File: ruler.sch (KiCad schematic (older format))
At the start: 80 parts, among them J1 USB_OTG, Q1 SOT23, Q2 SOT323, Q3 SOT883, Q4 SOT523, Q5 SOT223, Q6 SOT89, Q7 SuperSOT, SW1 KMR2, SW2 EVQPE1, SW3 B3U1000P, SW4 FSMCT, SW5 TL3315, SW6 FSM2JSM, SW7 JS202011SCQN, U1 QFN-0.5mm, U10 SOT963-6, U11 SSOP14, U12 SO16-L, U13 SOT666, U14 SOT1194, U15 SOT1333, U16 SOT669, U17 TSSOP 4.4x3mm, U18 SO4, U19 VSSOP, U2 LQFP, U3 SOIC, U4 BGA-0.8mm, U5 TSSOP 3x3mm, U6 MSOIC, U7 TSOP-0.95mm, U8 SOT23-6, U9 SOT23-8

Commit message: Add another switch
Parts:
- added LED?: 0201, KiCad/LEDs.pretty:LED_0201, symbol device:LED
- added R?: 1k, KiCad/Resistors_SMD.pretty:R_0402, symbol device:R
- added SW?: B3U, KiCad/Buttons_Switches_SMD.pretty:SW_SPST_EVQPE1, symbol switches:SW_Push
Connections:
- wire segments 78 -> 87
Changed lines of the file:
@@
 L device:D D5
 U 1 1 5AF4E276
-P 9625 1300
-F 0 "D5" V 9671 1221 50  0000 R CNN
-F 1 "SOD-323" V 9580 1221 50  0000 R CNN
-F 2 "KiCad/Diodes_SMD.pretty:D_SOD-323" H 9625 1300 50  0001 C CNN
-F 3 "" H 9625 1300 50  0001 C CNN
-	1    9625 1300
+P 4800 2750
+F 0 "D5" V 4846 2671 50  0000 R CNN
+F 1 "SOD-323" V 4755 2671 50  0000 R CNN
+F 2 "KiCad/Diodes_SMD.pretty:D_SOD-323" H 4800 2750 50  0001 C CNN
+F 3 "" H 4800 2750 50  0001 C CNN
+	1    4800 2750
 	0    -1   -1   0
 $EndComp
@@
 	1    0    0    -1
 $EndComp
+$Comp
+L device:R R?
+U 1 1 5B70AFDC
+P 4650 3150
+F 0 "R?" V 4730 3150 50  0000 C CNN
+F 1 "1k" V 4650 3150 50  0000 C CNN
+F 2 "KiCad/Resistors_SMD.pretty:R_0402" V 4580 3150 50  0001 C CNN
+F 3 "" H 4650 3150 50  0001 C CNN
+	1    4650 3150
+	1    0    0    -1
+$EndComp
+$Comp
+L device:LED LED?
+U 1 1 5B70AFE2
+P 4650 3575
+F 0 "LED?" H 4650 3675 50  0000 C CNN
+F 1 "0201" H 4650 3475 50  0000 C CNN
+F 2 "KiCad/LEDs.pretty:LED_0201" H 4650 3575 50  0001 C CNN
+F 3 "" H 4650 3575 50  0001 C CNN
+	1    4650 3575
+	0    -1   -1   0
+$EndComp
+$Comp
+L power:GND #PWR?
+U 1 1 5B70AFE8
+P 4650 3850
+F 0 "#PWR?" H 4650 3600 50  0001 C CNN
+F 1 "GND" H 4650 3700 50  0000 C CNN
+F 2 "" H 4650 3850 50  0001 C CNN
+F 3 "" H 4650 3850 50  0001 C CNN
+	1    4650 3850
+	1    0    0    -1
+$EndComp
+Wire Wire Line
+	4650 3725 4650 3850
+Wire Wire Line
+	4650 2925 4650 3000
+$Comp
+L switches:SW_Push SW?
+U 1 1 5B70AFF0
+P 4375 2925
+F 0 "SW?" H 4425 3025 50  0000 L CNN
+F 1 "B3U" H 4375 2865 50  0000 C CNN
+F 2 "KiCad/Buttons_Switches_SMD.pretty:SW_SPST_EVQPE1" H 4375 3125 50  0001 C CNN
+F 3 "" H 4375 3125 50  0001 C CNN
+	1    4375 2925
+	1    0    0    -1
+$EndComp
+Text GLabel 4100 2925 0    50   Input ~ 0
+SW_V+
+Wire Wire Line
+	4100 2925 4150 2925
+Text GLabel 4800 2400 1    50   Input ~ 0
+LED_V+
+Connection ~ 4150 2925
+Connection ~ 4575 2925
+Wire Wire Line
+	4575 2925 4650 2925
+Wire Wire Line
+	4800 2400 4800 2600
+Wire Wire Line
+	4800 2900 4800 2925
+Wire Wire Line
+	4800 2925 4650 2925
+Connection ~ 4650 2925
+Wire Wire Line
+	4650 3300 4650 3425
+Wire Wire Line
+	4175 2925 4150 2925
 $EndSCHEMATC

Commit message: Convert to kicad-5 properly?
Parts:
- C1, C2, C3, C4, C5, C6, C7, C8: symbol device:CP -> ruler-rescue:device_CP
- D1, D2, D3, D4, D5, D6: symbol device:D -> ruler-rescue:device_D
- DRAWING1, DRAWING10, DRAWING11, DRAWING12, DRAWING13, DRAWING14, DRAWING15, DRAWING16, DRAWING17, DRAWING18, DRAWING2, DRAWING3, DRAWING4, DRAWING5, DRAWING6, DRAWING9, U1, U10, U11, U12, U13, U14, U15, U16, U17, U18, U19, U2, U3, U4, U5, U6, U7, U8, U9: symbol conn:Conn_01x01 -> ruler-rescue:conn_Conn_01x01
- J1: symbol conn:USB_OTG -> ruler-rescue:conn_USB_OTG
- L1, L2, L3, L4, L5, L6: symbol pspice:INDUCTOR -> ruler-rescue:pspice_INDUCTOR
- LED1, LED2, LED3, LED4, LED5: symbol device:LED -> ruler-rescue:device_LED
- LED6: renamed from LED?; footprint KiCad/LEDs.pretty:LED_0201 -> KiCad/kicad-footprints/LED_SMD.pretty:LED_0201_0603Metric; symbol device:LED -> ruler-rescue:device_LED
- Q1, Q2, Q3, Q4, Q5, Q6, Q7: symbol device:Q_NMOS_DGS -> ruler-rescue:device_Q_NMOS_DGS
- R1, R2, R3, R4, R5: symbol device:R -> ruler-rescue:device_R
- R6: renamed from R?; footprint KiCad/Resistors_SMD.pretty:R_0402 -> KiCad/kicad-footprints/Resistor_SMD.pretty:R_01005_0402Metric; symbol device:R -> ruler-rescue:device_R
- SW1, SW2, SW3, SW6: symbol switches:SW_Push -> ruler-rescue:switches_SW_Push
- SW4, SW5: symbol switches:SW_Push_Dual -> ruler-rescue:switches_SW_Push_Dual
- SW7: symbol Switch:SW_DPDT_x2 -> ruler-rescue:Switch_SW_DPDT_x2
- SW8: renamed from SW?; symbol switches:SW_Push -> ruler-rescue:switches_SW_Push
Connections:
- wire segments 87 -> 86

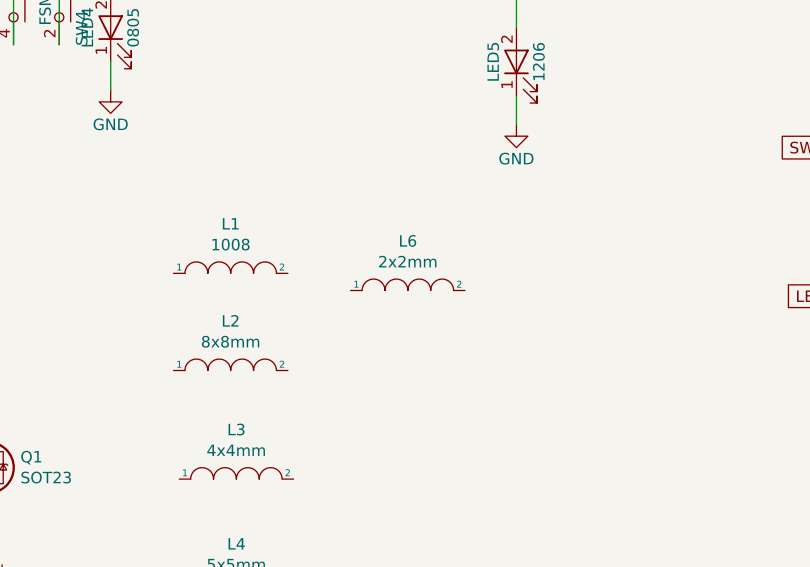
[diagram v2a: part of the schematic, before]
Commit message: Add a tactile switch and 0201 LED
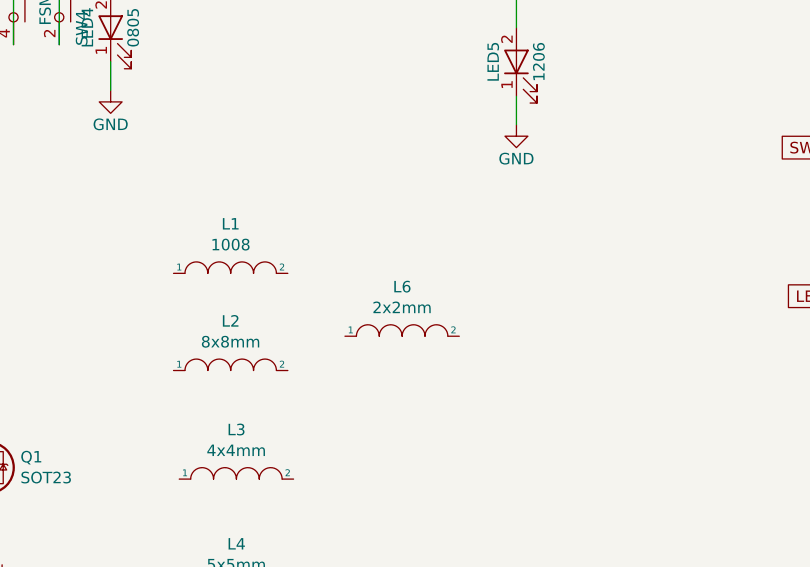
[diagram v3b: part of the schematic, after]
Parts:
- SW8: footprint KiCad/Buttons_Switches_SMD.pretty:SW_SPST_EVQPE1 -> brunoeagle/kicad-open-modules:B3U-1000P
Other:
- moved on the sheet: L6
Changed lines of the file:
@@
 L ruler-rescue:pspice_INDUCTOR L6
 U 1 1 5AF4B711
-P 8450 3125
-F 0 "L6" H 8450 3340 50  0000 C CNN
-F 1 "2x2mm" H 8450 3249 50  0000 C CNN
-F 2 "KiCad/Inductors.pretty:Inductor_Taiyo-Yuden_NR-20xx" H 8450 3125 50  0001 C CNN
-F 3 "" H 8450 3125 50  0001 C CNN
-	1    8450 3125
+P 8425 3325
+F 0 "L6" H 8425 3540 50  0000 C CNN
+F 1 "2x2mm" H 8425 3449 50  0000 C CNN
+F 2 "KiCad/Inductors.pretty:Inductor_Taiyo-Yuden_NR-20xx" H 8425 3325 50  0001 C CNN
+F 3 "" H 8425 3325 50  0001 C CNN
+	1    8425 3325
 	1    0    0    -1
 $EndComp
@@
 F 0 "SW8" H 4425 3025 50  0000 L CNN
 F 1 "B3U" H 4375 2865 50  0000 C CNN
-F 2 "KiCad/Buttons_Switches_SMD.pretty:SW_SPST_EVQPE1" H 4375 3125 50  0001 C CNN
+F 2 "brunoeagle/kicad-open-modules:B3U-1000P" H 4375 3125 50  0001 C CNN
 F 3 "" H 4375 3125 50  0001 C CNN
 	1    4375 2925

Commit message: Route
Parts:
- removed DRAWING14: Conn_01x01, drawings:mouse, symbol ruler-rescue:conn_Conn_01x01
- removed DRAWING15: Conn_01x01, drawings:chipmunk, symbol ruler-rescue:conn_Conn_01x01
- removed DRAWING16: Conn_01x01, drawings:weasel, symbol ruler-rescue:conn_Conn_01x01
- removed DRAWING17, DRAWING18: Conn_01x01, drawings:ant, symbol ruler-rescue:conn_Conn_01x01
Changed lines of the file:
@@
-$EndComp
-$Comp
-L ruler-rescue:conn_Conn_01x01 DRAWING14
-U 1 1 5AF42BAF
-P 9200 5750
-F 0 "DRAWING14" H 9200 5850 50  0000 C CNN
-F 1 "Conn_01x01" H 9200 5650 50  0000 C CNN
-F 2 "drawings:mouse" H 9200 5750 50  0001 C CNN
-F 3 "" H 9200 5750 50  0001 C CNN
-	1    9200 5750
-	1    0    0    -1
 $EndComp
 $Comp
@@
 $EndComp
 $Comp
-L ruler-rescue:conn_Conn_01x01 DRAWING15
-U 1 1 5B01E53E
-P 7200 6250
-F 0 "DRAWING15" H 7200 6350 50  0000 C CNN
-F 1 "Conn_01x01" H 7200 6150 50  0000 C CNN
-F 2 "drawings:chipmunk" H 7200 6250 50  0001 C CNN
-F 3 "" H 7200 6250 50  0001 C CNN
-	1    7200 6250
-	1    0    0    -1
-$EndComp
-$Comp
-L ruler-rescue:conn_Conn_01x01 DRAWING16
-U 1 1 5B01F029
-P 7225 5900
-F 0 "DRAWING16" H 7225 6000 50  0000 C CNN
-F 1 "Conn_01x01" H 7225 5800 50  0000 C CNN
-F 2 "drawings:weasel" H 7225 5900 50  0001 C CNN
-F 3 "" H 7225 5900 50  0001 C CNN
-	1    7225 5900
-	1    0    0    -1
-$EndComp
-$Comp
 L ruler-rescue:conn_Conn_01x01 U14
 U 1 1 5B01F626
@@
 	1    0    0    -1
 $EndComp
-$Comp
-L ruler-rescue:conn_Conn_01x01 DRAWING17
-U 1 1 5B026222
-P 10725 5450
-F 0 "DRAWING17" H 10725 5550 50  0000 C CNN
-F 1 "Conn_01x01" H 10725 5350 50  0000 C CNN
-F 2 "drawings:ant" H 10725 5450 50  0001 C CNN
-F 3 "" H 10725 5450 50  0001 C CNN
-	1    10725 5450
-	1    0    0    -1
-$EndComp
-$Comp
-L ruler-rescue:conn_Conn_01x01 DRAWING18
-U 1 1 5B0267EF
-P 10075 5375
-F 0 "DRAWING18" H 10075 5475 50  0000 C CNN
-F 1 "Conn_01x01" H 10075 5275 50  0000 C CNN
-F 2 "drawings:ant" H 10075 5375 50  0001 C CNN
-F 3 "" H 10075 5375 50  0001 C CNN
-	1    10075 5375
-	1    0    0    -1
-$EndComp

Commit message: Move some stuff around and plot
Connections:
- net LED_V+: now also D6.2 (A); no longer D5.2 (A)
- net at R1.1, SW8.2: now also D6.1 (K); no longer D5.1 (K)
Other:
- moved on the sheet: D5, D6
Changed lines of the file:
@@
 L ruler-rescue:device_D D5
 U 1 1 5AF4E276
-P 4800 2750
-F 0 "D5" V 4846 2671 50  0000 R CNN
-F 1 "SOD-323" V 4755 2671 50  0000 R CNN
-F 2 "KiCad/Diodes_SMD.pretty:D_SOD-323" H 4800 2750 50  0001 C CNN
-F 3 "" H 4800 2750 50  0001 C CNN
-	1    4800 2750
+P 9825 1825
+F 0 "D5" V 9871 1746 50  0000 R CNN
+F 1 "SOD-323" V 9780 1746 50  0000 R CNN
+F 2 "KiCad/Diodes_SMD.pretty:D_SOD-323" H 9825 1825 50  0001 C CNN
+F 3 "" H 9825 1825 50  0001 C CNN
+	1    9825 1825
 	0    -1   -1   0
 $EndComp
@@
 L ruler-rescue:device_D D6
 U 1 1 5AF4E2E0
-P 10225 1275
-F 0 "D6" V 10271 1196 50  0000 R CNN
-F 1 "SOD-523" V 10180 1196 50  0000 R CNN
-F 2 "KiCad/Diodes_SMD.pretty:D_SOD-523" H 10225 1275 50  0001 C CNN
-F 3 "" H 10225 1275 50  0001 C CNN
-	1    10225 1275
+P 4800 2750
+F 0 "D6" V 4846 2671 50  0000 R CNN
+F 1 "SOD-523" V 4755 2671 50  0000 R CNN
+F 2 "KiCad/Diodes_SMD.pretty:D_SOD-523" H 4800 2750 50  0001 C CNN
+F 3 "" H 4800 2750 50  0001 C CNN
+	1    4800 2750
 	0    -1   -1   0
 $EndComp

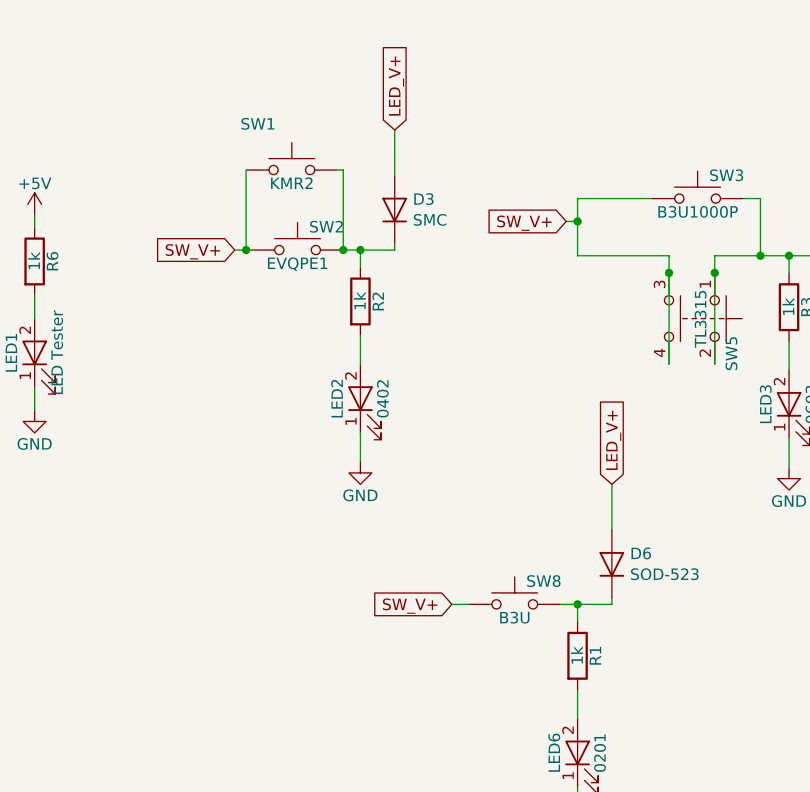
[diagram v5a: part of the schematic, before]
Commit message: Switch out second b3u button
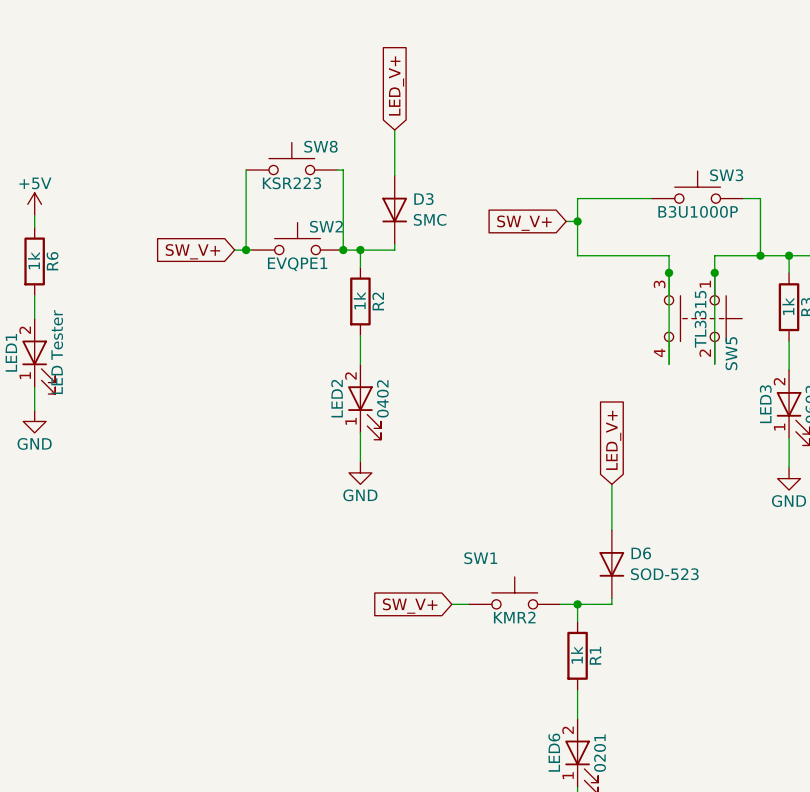
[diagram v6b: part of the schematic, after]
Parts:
- SW8: value B3U -> KSR223; footprint brunoeagle/kicad-open-modules:B3U-1000P -> OpenMusicKontrollers/omk.pretty:KSR
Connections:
- net at D3.1 (K), R2.1, SW2.2: now also SW8.2; no longer SW1.2
- net at D6.1 (K), R1.1: now also SW1.2; no longer SW8.2
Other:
- moved on the sheet: SW1, SW8
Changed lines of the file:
@@
 L ruler-rescue:switches_SW_Push SW1
 U 1 1 5AF21638
-P 3400 1025
-F 0 "SW1" H 3175 1225 50  0000 L CNN
-F 1 "KMR2" H 3400 965 50  0000 C CNN
-F 2 "KiCad/Buttons_Switches_SMD.pretty:SW_SPST_KMR2" H 3400 1225 50  0001 C CNN
-F 3 "" H 3400 1225 50  0001 C CNN
-	1    3400 1025
+P 4375 2925
+F 0 "SW1" H 4150 3125 50  0000 L CNN
+F 1 "KMR2" H 4375 2865 50  0000 C CNN
+F 2 "KiCad/Buttons_Switches_SMD.pretty:SW_SPST_KMR2" H 4375 3125 50  0001 C CNN
+F 3 "" H 4375 3125 50  0001 C CNN
+	1    4375 2925
 	1    0    0    -1
 $EndComp
@@
 L ruler-rescue:switches_SW_Push SW8
 U 1 1 5B70AFF0
-P 4375 2925
-F 0 "SW8" H 4425 3025 50  0000 L CNN
-F 1 "B3U" H 4375 2865 50  0000 C CNN
-F 2 "brunoeagle/kicad-open-modules:B3U-1000P" H 4375 3125 50  0001 C CNN
-F 3 "" H 4375 3125 50  0001 C CNN
-	1    4375 2925
-	1    0    0    -1
-$EndComp
+P 3400 1025
+F 0 "SW8" H 3450 1125 50  0000 L CNN
+F 1 "KSR223" H 3400 965 50  0000 C CNN
+F 2 "OpenMusicKontrollers/omk.pretty:KSR" H 3400 1225 50  0001 C CNN
+F 3 "" H 3400 1225 50  0001 C CNN
+	1    3400 1025
+	1    0    0    -1
+$EndComp

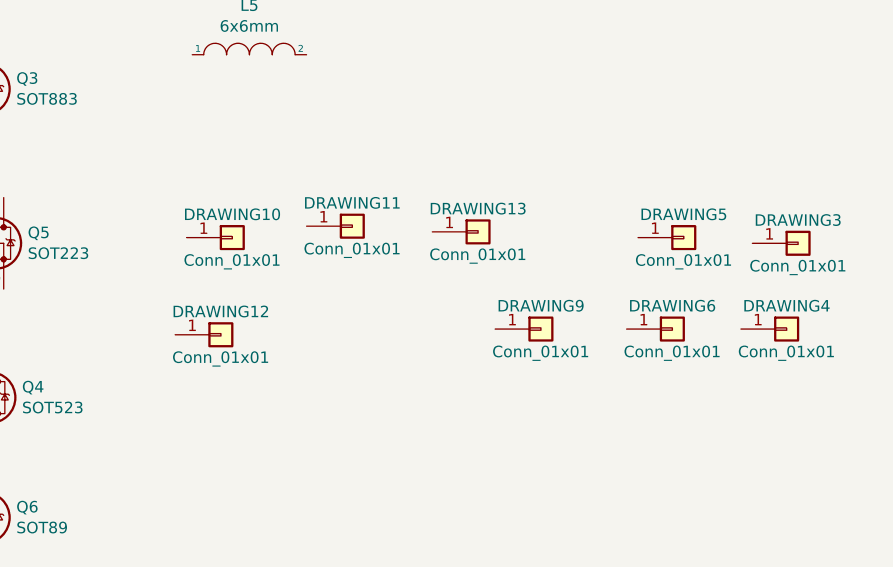
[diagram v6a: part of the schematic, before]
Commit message: Duplicate the layout into the frame
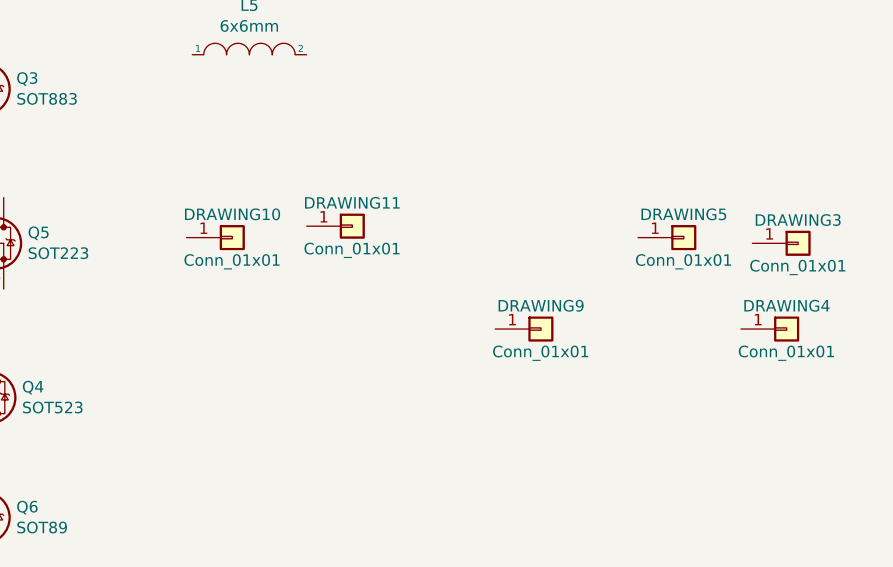
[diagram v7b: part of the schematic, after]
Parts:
- removed DRAWING12: Conn_01x01, drawings:vscore, symbol ruler-rescue:conn_Conn_01x01
- removed DRAWING13: Conn_01x01, drawings:mouse_bites, symbol ruler-rescue:conn_Conn_01x01
- removed DRAWING6: Conn_01x01, drawings:capacitors_text, symbol ruler-rescue:conn_Conn_01x01
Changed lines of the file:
@@
-$EndComp
-$Comp
-L ruler-rescue:conn_Conn_01x01 DRAWING6
-U 1 1 5AF3813A
-P 9650 6200
-F 0 "DRAWING6" H 9650 6300 50  0000 C CNN
-F 1 "Conn_01x01" H 9650 6100 50  0000 C CNN
-F 2 "drawings:capacitors_text" H 9650 6200 50  0001 C CNN
-F 3 "" H 9650 6200 50  0001 C CNN
-	1    9650 6200
-	1    0    0    -1
 $EndComp
 $Comp
@@
 $EndComp
 $Comp
-L ruler-rescue:conn_Conn_01x01 DRAWING12
-U 1 1 5AF3A08D
-P 7675 6225
-F 0 "DRAWING12" H 7675 6325 50  0000 C CNN
-F 1 "Conn_01x01" H 7675 6125 50  0000 C CNN
-F 2 "drawings:vscore" H 7675 6225 50  0001 C CNN
-F 3 "" H 7675 6225 50  0001 C CNN
-	1    7675 6225
-	1    0    0    -1
-$EndComp
-$Comp
 L ruler-rescue:conn_Conn_01x01 U6
 U 1 1 5AF3E368
@@
 	1    0    0    -1
 $EndComp
-$Comp
-L ruler-rescue:conn_Conn_01x01 DRAWING13
-U 1 1 5AF42ADB
-P 8800 5775
-F 0 "DRAWING13" H 8800 5875 50  0000 C CNN
-F 1 "Conn_01x01" H 8800 5675 50  0000 C CNN
-F 2 "drawings:mouse_bites" H 8800 5775 50  0001 C CNN
-F 3 "" H 8800 5775 50  0001 C CNN
-	1    8800 5775
-	1    0    0    -1
-$EndComp
